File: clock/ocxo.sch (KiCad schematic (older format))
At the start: 33 parts

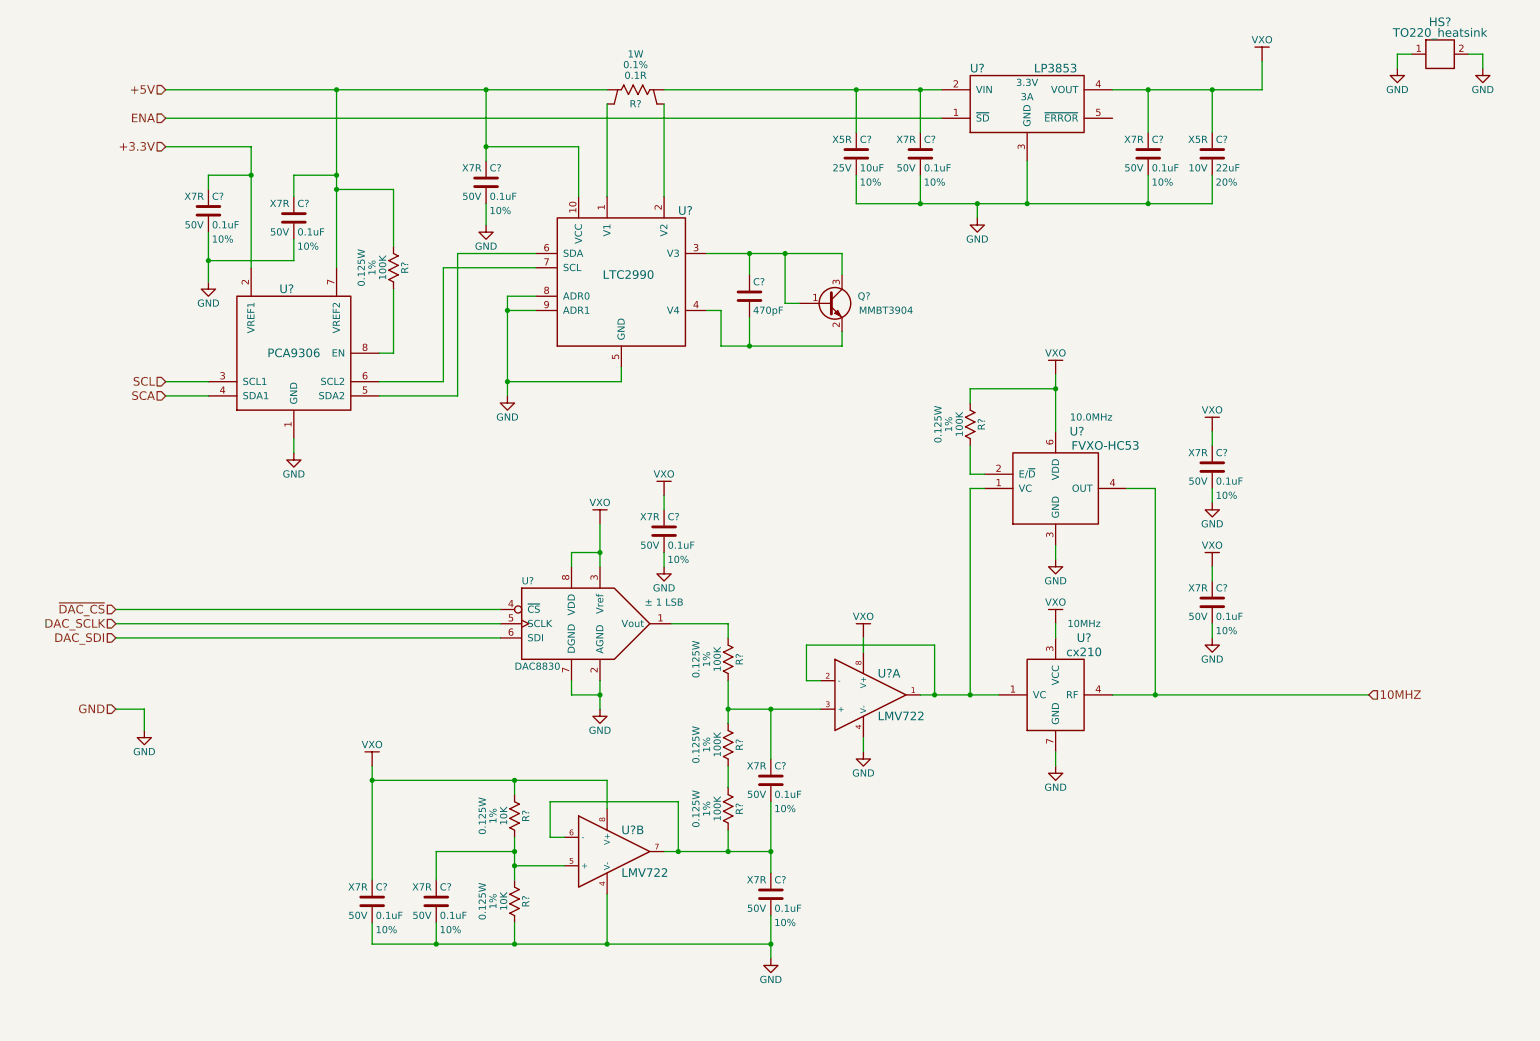
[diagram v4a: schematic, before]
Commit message: Add proper loading and buffer to the OCXO output.
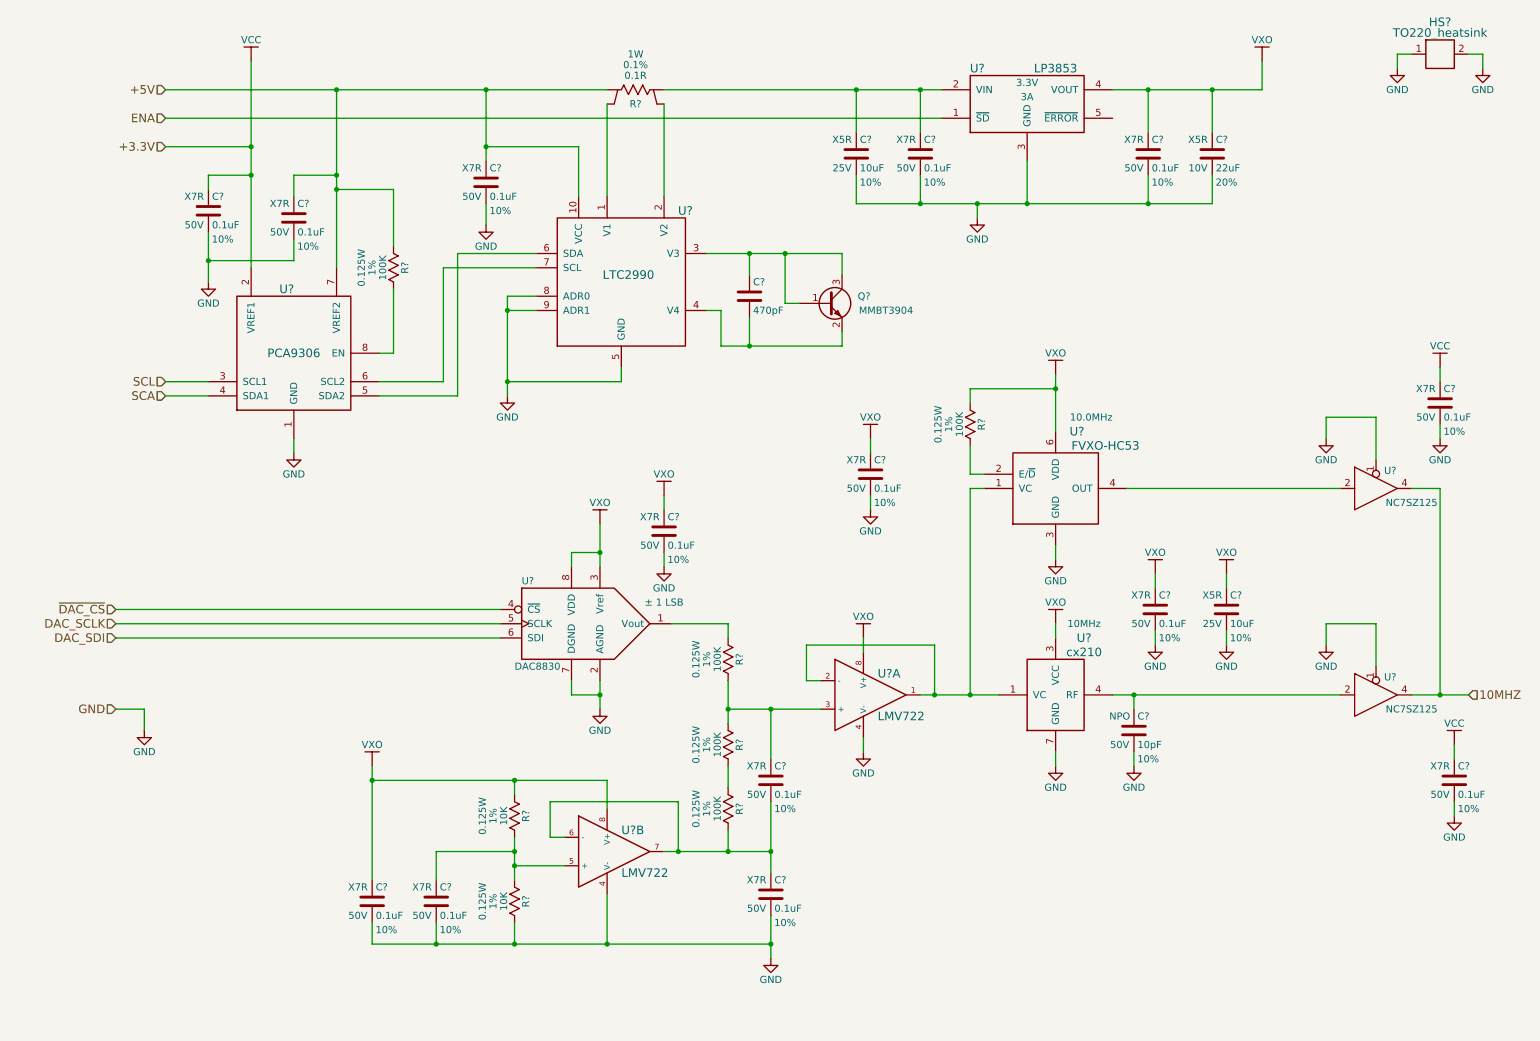
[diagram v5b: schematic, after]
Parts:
- added C?: 10pF, Capacitors_SMD:C_0805_HandSoldering, symbol C
- added C?: 10uF, Capacitors_SMD:C_1206_HandSoldering, symbol C
- added C? (x2): 0.1uF, Capacitors_SMD:C_0805_HandSoldering, symbol C
- added U? (x2): NC7SZ125, symbol NC7SZ125
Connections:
- net 10MHZ: now also U?.4, U?.4; no longer U?.4 (OUT), U?.4 (RF)
- net GND: now also C?.2, C?.2, C?.2, C?.2, U?.1, U?.1, U?.3 (GND), U?.3 (GND)
- net VXO: now also C?.1
- net +3.3V renamed VCC
- net VCC: now also C?.1, C?.1, U?.5 (VCC), U?.5 (VCC)
- new net: U?.2, U?.4 (OUT)
- new net: C?.1, U?.2, U?.4 (RF)
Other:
- moved on the sheet: C?

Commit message: Fan and power connectors.
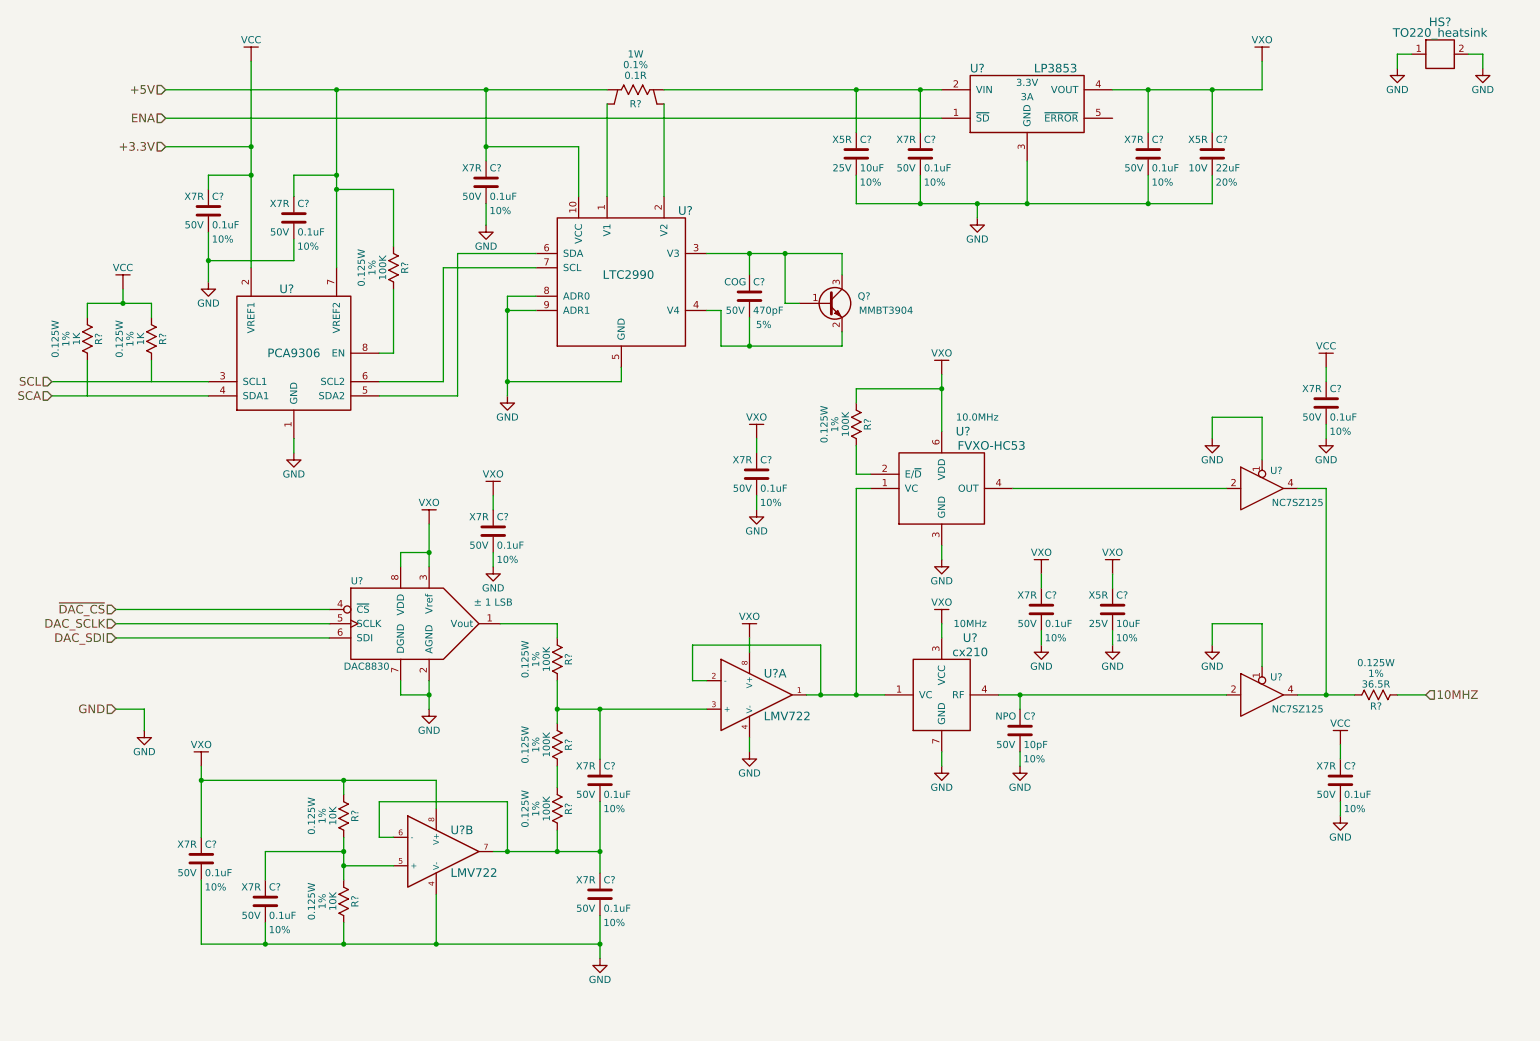
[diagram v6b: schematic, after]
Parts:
- removed C?: 470pF, symbol C
- added C?: 470pF, Capacitors_SMD:C_0805_HandSoldering, symbol C
- added R?: 36.5R, Resistors_SMD:R_0805_HandSoldering, symbol R_local
- added R? (x2): 1K, Resistors_SMD:R_0805_HandSoldering, symbol R_local
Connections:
- net 10MHZ: now also R?.1; no longer U?.4, U?.4
- net VCC: now also R?.1, R?.1
- net at Q?.1 (B), Q?.3 (C), U?.3 (V3): now also C?.1
- net at Q?.2 (E), U?.4 (V4): now also C?.2
- new net: R?.2, U?.4, U?.4
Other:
- moved on the sheet: C?, R?, U?, U?A, U?B

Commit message: Correct footprint selection. Start pcb. Add BOM files.
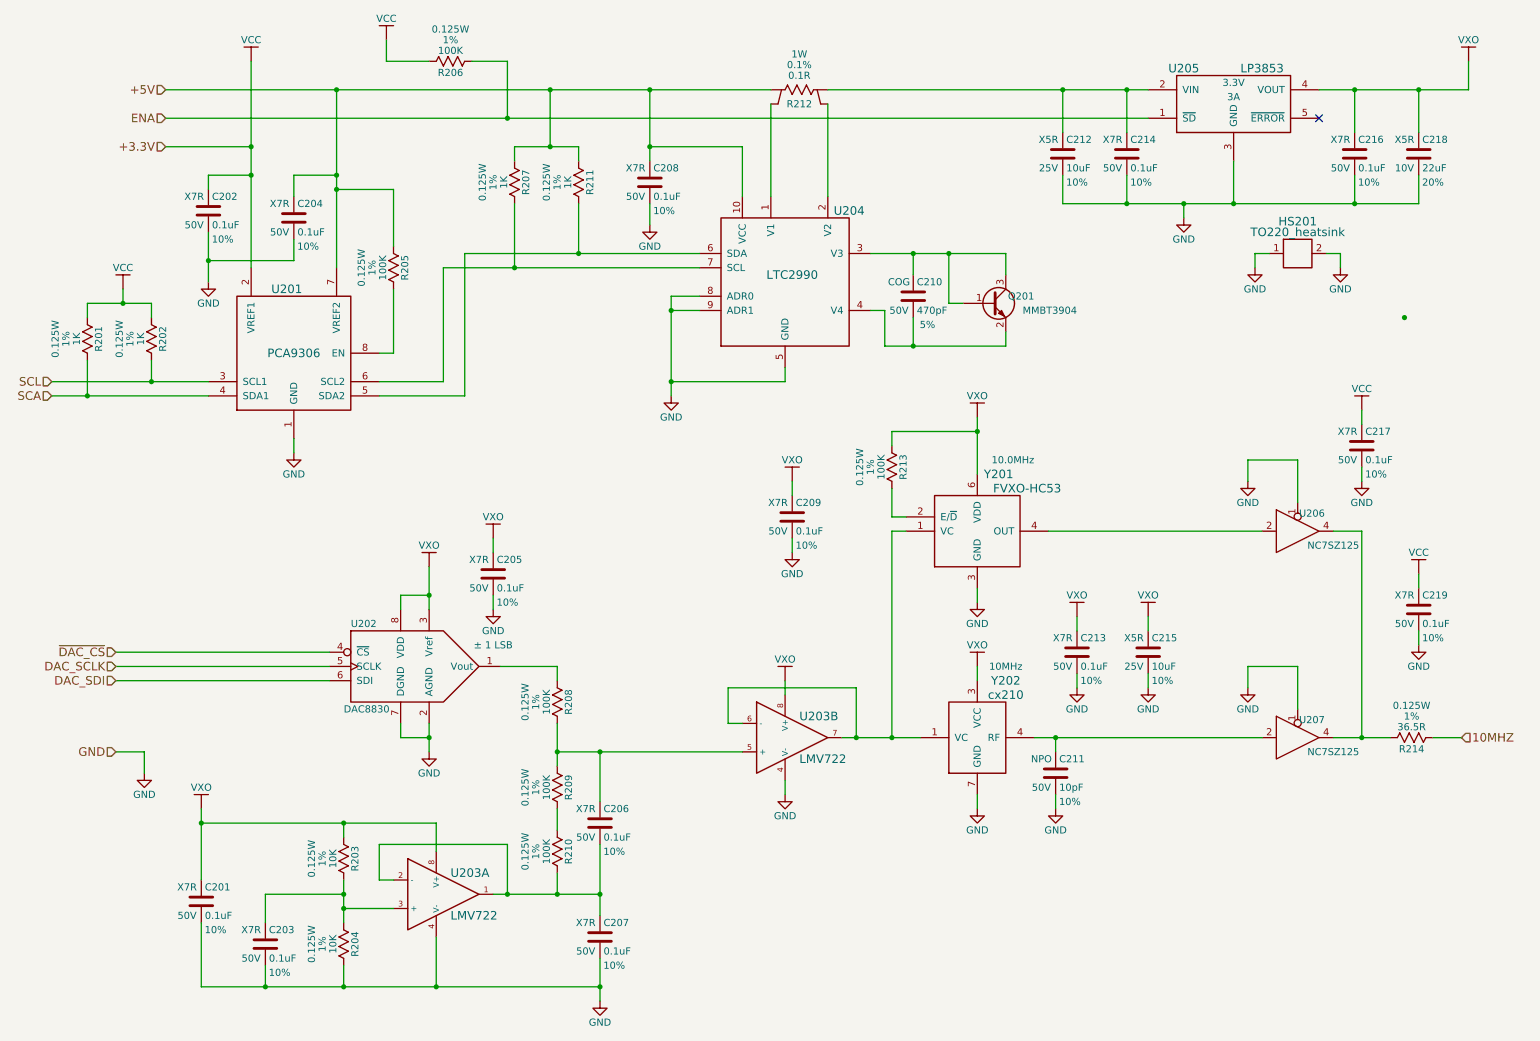
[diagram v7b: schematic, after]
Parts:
- removed U?: FVXO-HC53, symbol FVXO-HC53
- removed U?: cx210, symbol cx210
- added R206: 100K, Resistors_SMD:R_0805_HandSoldering, symbol R_local
- added R207, R211: 1K, Resistors_SMD:R_0805_HandSoldering, symbol R_local
- added Y201: FVXO-HC53, local:FVXO_HandSoldering, symbol FVXO-HC53
- added Y202: cx210, local:CX210_HandSoldering, symbol cx210
- HS201: renamed from HS?; footprint (none) -> local:Heatsink_581x
- Q201: renamed from Q?; footprint (none) -> Housings_SOT-23_SOT-143_TSOT-6:SOT-23_Handsoldering
- R212: renamed from R?; footprint (none) -> local:CSM2512_0R007_0R2
- U201: renamed from U?; footprint (none) -> Housings_SSOP:MSOP-8_3x3mm_Pitch0.65mm
- U202, U203: renamed from U?; footprint (none) -> Housings_SOIC:SOIC-8_3.9x4.9mm_Pitch1.27mm
- U204: renamed from U?; footprint (none) -> Housings_SSOP:MSOP-10_3x3mm_Pitch0.5mm
- U205: renamed from U?; footprint (none) -> local:TO220-5-Vertical_NDH
- U206, U207: renamed from U?; footprint (none) -> local:SOT-23-5_1.6x2.9mm_Pitch0.95mm
- gave numbers to parts that had none: 29
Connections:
- net +5V: now also R207.1, R211.1
- net ENA: now also R206.1
- net GND: now also Y201.3 (GND), Y202.7 (GND)
- net SCA: now also R201.2
- net SCL: now also R202.2
- net VCC: now also R206.2
- net VXO: now also Y201.6 (VDD), Y202.3 (VCC)
- net at C203.1, R203.2, R204.1: now also U203.3 (+); no longer U203.5 (+)
- net at C206.2, C207.1, R210.2: now also U203.1, U203.2 (-); no longer U203.6 (-), U203.7
- net at C206.1, R208.2, R209.1: now also U203.5 (+); no longer U203.3 (+)
- net at R213.2: now also Y201.2 (E/~D~)
- net at U201.5 (SDA2), U204.6 (SDA): now also R211.2
- net at U201.6 (SCL2), U204.7 (SCL): now also R207.2
- net at U206.2: now also Y201.4 (OUT)
- net at C211.1, U207.2: now also Y202.4 (RF)
- new net: U203.6 (-), U203.7, Y201.1 (VC), Y202.1 (VC)
- no-connect marks 0 -> 1
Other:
- moved on the sheet: C201, C203, C205, C206, C207, C208, C209, C210, C211, C212, C213, C214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
